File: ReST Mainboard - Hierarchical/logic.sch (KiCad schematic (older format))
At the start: 19 parts, among them IC1 AT24C256, P15 USB_OTG, U10 USBLC6-2, U9 STM32F10x/STM32F4x, X1 Crystal_Small

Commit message: started routing
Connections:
- net USB_D+ renamed USBP_D+
- net USB_D- renamed USBP_D-
- net USB_DM_- renamed USB_MCU-
- net USB_DP_+ renamed USB_MCU+
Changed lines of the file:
@@
 USB INTERFACE
 Text Label 9150 450  0    39   ~ 0
-USB_D+
+USBP_D+
 Text Label 9100 550  0    39   ~ 0
-USB_D-
+USBP_D-
 Text Label 10500 450  1    39   ~ 0
 USBR+
@@
 SPI_CS0
 Text GLabel 6700 1850 2    39   Input ~ 0
-USB_DP_+
+USB_MCU+
 Text GLabel 6700 1750 2    39   Input ~ 0
-USB_DM_-
+USB_MCU-
 $Comp
 L AT24C256 IC1
@@
 RESET
 Text GLabel 10900 450  2    39   Input ~ 0
-USB_DP_+
+USB_MCU+
 Text GLabel 10900 550  2    39   Input ~ 0
-USB_DM_-
+USB_MCU-
 Text GLabel 3700 1550 0    39   Input ~ 0
 P_VCAP_2

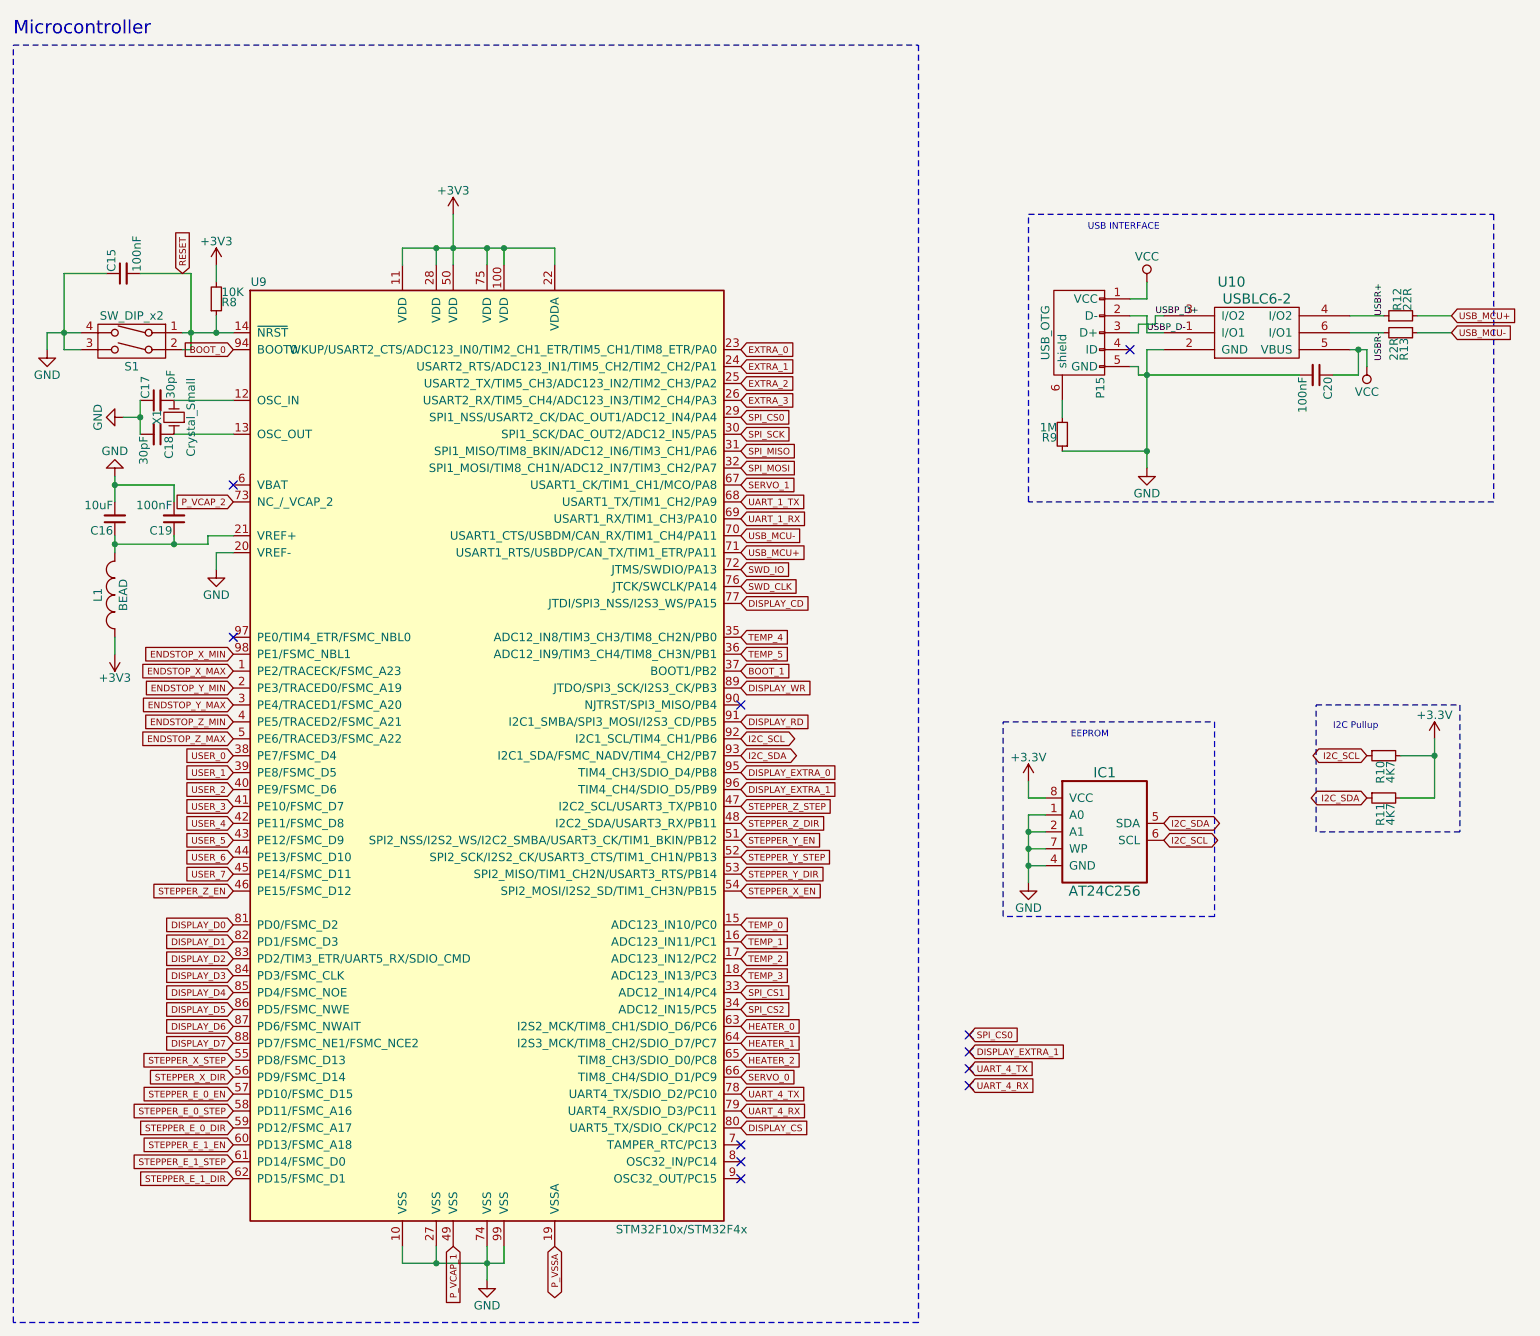
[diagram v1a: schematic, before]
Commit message: Mostly finished with main PCB. Only need to work the High Current Stuff out. On Vacation for now
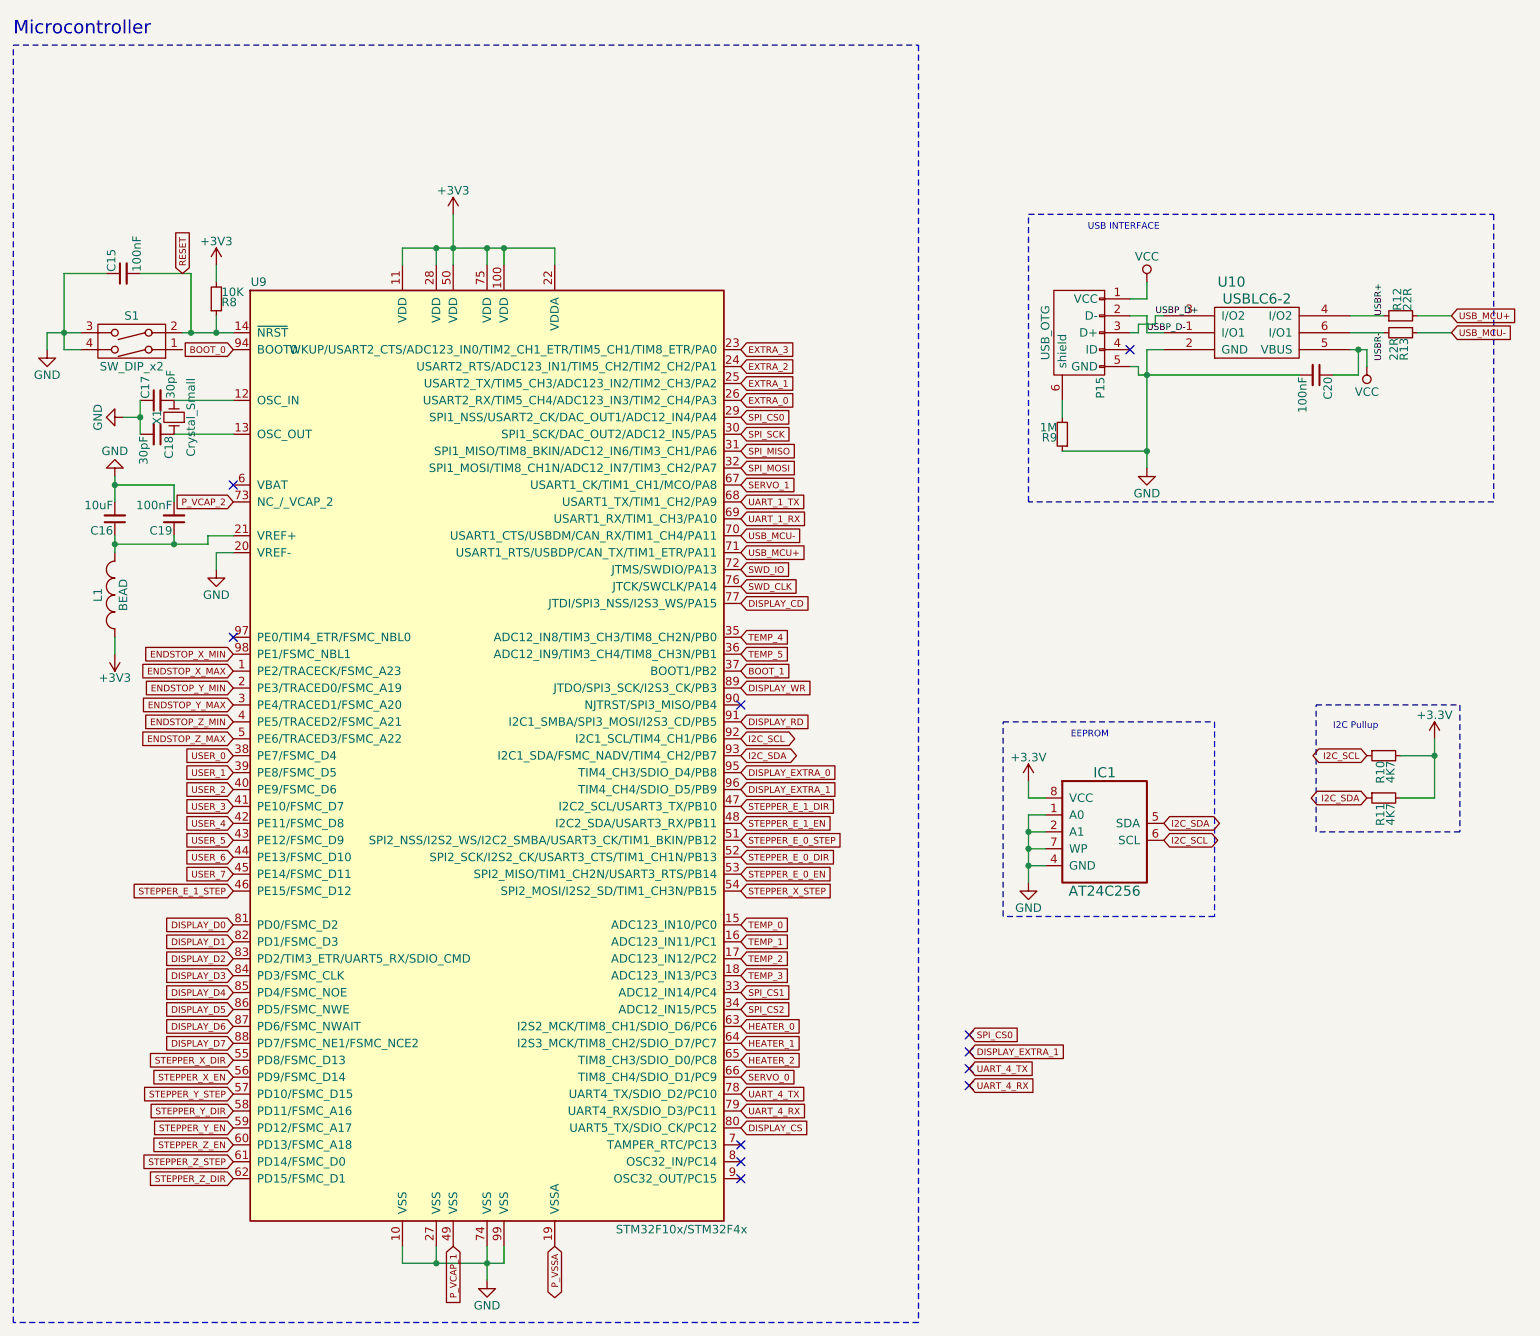
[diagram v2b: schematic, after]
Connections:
- net EXTRA_0: now also U9.26 (USART2_RX/TIM5_CH4/ADC123_IN3/TIM2_CH4/PA3); no longer U9.23 (WKUP/USART2_CTS/ADC123_IN0/TIM2_CH1_ETR/TIM5_CH1/TIM8_ETR/PA0)
- net EXTRA_1: now also U9.25 (USART2_TX/TIM5_CH3/ADC123_IN2/TIM2_CH3/PA2); no longer U9.24 (USART2_RTS/ADC123_IN1/TIM5_CH2/TIM2_CH2/PA1)
- net EXTRA_2: now also U9.24 (USART2_RTS/ADC123_IN1/TIM5_CH2/TIM2_CH2/PA1); no longer U9.25 (USART2_TX/TIM5_CH3/ADC123_IN2/TIM2_CH3/PA2)
- net EXTRA_3: now also U9.23 (WKUP/USART2_CTS/ADC123_IN0/TIM2_CH1_ETR/TIM5_CH1/TIM8_ETR/PA0); no longer U9.26 (USART2_RX/TIM5_CH4/ADC123_IN3/TIM2_CH4/PA3)
- net RESET: no longer S1.1
- net STEPPER_E_0_DIR: now also U9.52 (SPI2_SCK/I2S2_CK/USART3_CTS/TIM1_CH1N/PB13); no longer U9.59 (PD12/FSMC_A17)
- net STEPPER_E_0_EN: now also U9.53 (SPI2_MISO/TIM1_CH2N/USART3_RTS/PB14); no longer U9.57 (PD10/FSMC_D15)
- net STEPPER_E_0_STEP: now also U9.51 (SPI2_NSS/I2S2_WS/I2C2_SMBA/USART3_CK/TIM1_BKIN/PB12); no longer U9.58 (PD11/FSMC_A16)
- net STEPPER_E_1_DIR: now also U9.47 (I2C2_SCL/USART3_TX/PB10); no longer U9.62 (PD15/FSMC_D1)
- net STEPPER_E_1_EN: now also U9.48 (I2C2_SDA/USART3_RX/PB11); no longer U9.60 (PD13/FSMC_A18)
- net STEPPER_E_1_STEP: now also U9.46 (PE15/FSMC_D12); no longer U9.61 (PD14/FSMC_D0)
- net STEPPER_X_DIR: now also U9.55 (PD8/FSMC_D13); no longer U9.56 (PD9/FSMC_D14)
- net STEPPER_X_EN: now also U9.56 (PD9/FSMC_D14); no longer U9.54 (SPI2_MOSI/I2S2_SD/TIM1_CH3N/PB15)
- net STEPPER_X_STEP: now also U9.54 (SPI2_MOSI/I2S2_SD/TIM1_CH3N/PB15); no longer U9.55 (PD8/FSMC_D13)
- net STEPPER_Y_DIR: now also U9.58 (PD11/FSMC_A16); no longer U9.53 (SPI2_MISO/TIM1_CH2N/USART3_RTS/PB14)
- net STEPPER_Y_EN: now also U9.59 (PD12/FSMC_A17); no longer U9.51 (SPI2_NSS/I2S2_WS/I2C2_SMBA/USART3_CK/TIM1_BKIN/PB12)
- net STEPPER_Y_STEP: now also U9.57 (PD10/FSMC_D15); no longer U9.52 (SPI2_SCK/I2S2_CK/USART3_CTS/TIM1_CH1N/PB13)
- net STEPPER_Z_DIR: now also U9.62 (PD15/FSMC_D1); no longer U9.48 (I2C2_SDA/USART3_RX/PB11)
- net STEPPER_Z_EN: now also U9.60 (PD13/FSMC_A18); no longer U9.46 (PE15/FSMC_D12)
- net STEPPER_Z_STEP: now also U9.61 (PD14/FSMC_D0); no longer U9.47 (I2C2_SCL/USART3_TX/PB10)

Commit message: electrically finished. in the works of the silkscreening.
Schematic for SD Card Adapter and a RepRapDiscount-Adapter in the works. but not in this commit
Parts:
- P15: footprint Connect:USB_Mini-B -> ReST-Library:USB_Mini-B
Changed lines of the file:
@@
 F 0 "P15" H 9025 425 50  0000 C CNN
 F 1 "USB_OTG" H 8700 750 50  0000 C CNN
-F 2 "Connect:USB_Mini-B" V 8650 450 50  0001 C CNN
+F 2 "ReST-Library:USB_Mini-B" V 8650 450 50  0001 C CNN
 F 3 "" V 8650 450 50  0000 C CNN
 	1    8700 550

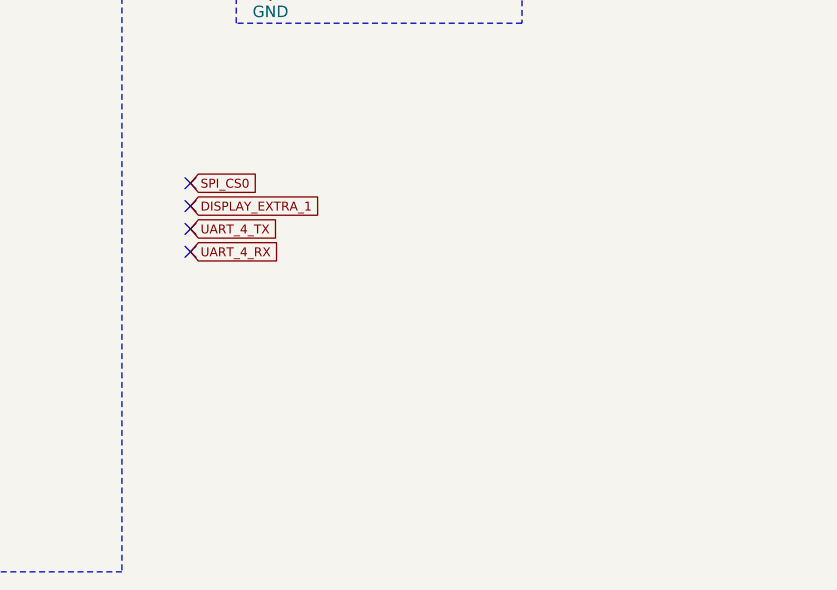
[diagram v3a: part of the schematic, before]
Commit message: added ESP-01 Support
Afterthought, completely forgot about it
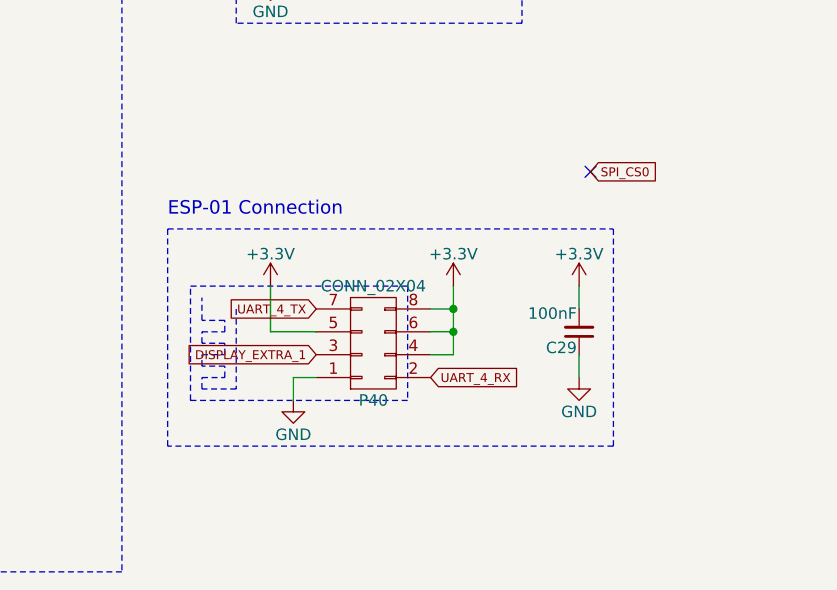
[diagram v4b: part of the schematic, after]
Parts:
- added C29: 100nF, Capacitors_SMD:C_0805_HandSoldering, symbol C_Small
- added P40: CONN_02X04, Pin_Headers:Pin_Header_Straight_2x04, symbol CONN_02X04
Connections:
- net +3V3: now also C29.2, P40.4 (P4), P40.5 (P5), P40.6 (P6), P40.8 (P8)
- net DISPLAY_EXTRA_1: now also P40.3 (P3)
- net GND: now also C29.1, P40.1 (P1)
- net UART_4_RX: now also P40.2 (P2)
- net UART_4_TX: now also P40.7 (P7)
- no-connect marks 11 -> 8
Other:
- note added: "ESP-01 Connection"
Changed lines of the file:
@@
 $EndDescr
 $Comp
-L +3.3V #PWR0120
+L +3.3V #PWR121
 U 1 1 5778C1BC
 P 8400 3200
-F 0 "#PWR0120" H 8400 3050 50  0001 C CNN
+F 0 "#PWR121" H 8400 3050 50  0001 C CNN
 F 1 "+3.3V" H 8400 3340 50  0000 C CNN
 F 2 "" H 8400 3200 50  0000 C CNN
@@
 $EndComp
 $Comp
-L GND #PWR0121
+L GND #PWR122
 U 1 1 5778C1C2
 P 8400 3800
-F 0 "#PWR0121" H 8400 3550 50  0001 C CNN
+F 0 "#PWR122" H 8400 3550 50  0001 C CNN
 F 1 "GND" H 8400 3650 50  0000 C CNN
 F 2 "" H 8400 3800 50  0000 C CNN
@@
 I2C_SDA
 $Comp
-L +3.3V #PWR0122
+L +3.3V #PWR131
 U 1 1 5778E907
 P 10800 2950
-F 0 "#PWR0122" H 10800 2800 50  0001 C CNN
+F 0 "#PWR131" H 10800 2800 50  0001 C CNN
 F 1 "+3.3V" H 10800 3090 50  0000 C CNN
 F 2 "" H 10800 2950 50  0000 C CNN
@@
 I2C_SDA
 $Comp
-L +3V3 #PWR0123
+L +3V3 #PWR119
 U 1 1 57791FB8
 P 5000 -150
-F 0 "#PWR0123" H 5000 -300 50  0001 C CNN
+F 0 "#PWR119" H 5000 -300 50  0001 C CNN
 F 1 "+3V3" H 5000 -10 50  0000 C CNN
 F 2 "" H 5000 -150 50  0000 C CNN
@@
 $EndComp
 $Comp
-L GND #PWR0124
+L GND #PWR116
 U 1 1 57791FBE
 P 3050 1050
-F 0 "#PWR0124" H 3050 800 50  0001 C CNN
+F 0 "#PWR116" H 3050 800 50  0001 C CNN
 F 1 "GND" H 3050 900 50  0000 C CNN
 F 2 "" H 3050 1050 50  0000 C CNN
@@
 $EndComp
 $Comp
-L GND #PWR0125
+L GND #PWR120
 U 1 1 57791FC4
 P 5200 6150
-F 0 "#PWR0125" H 5200 5900 50  0001 C CNN
+F 0 "#PWR120" H 5200 5900 50  0001 C CNN
 F 1 "GND" H 5200 6000 50  0000 C CNN
 F 2 "" H 5200 6150 50  0000 C CNN
@@
 $EndComp
 $Comp
-L GND #PWR0126
+L GND #PWR118
 U 1 1 57791FDF
 P 3600 1950
-F 0 "#PWR0126" H 3600 1700 50  0001 C CNN
+F 0 "#PWR118" H 3600 1700 50  0001 C CNN
 F 1 "GND" H 3600 1800 50  0000 C CNN
 F 2 "" H 3600 1950 50  0000 C CNN
@@
 $EndComp
 $Comp
-L +3V3 #PWR0127
+L +3V3 #PWR117
 U 1 1 57791FED
 P 3600 150
-F 0 "#PWR0127" H 3600 0   50  0001 C CNN
+F 0 "#PWR117" H 3600 0   50  0001 C CNN
 F 1 "+3V3" H 3600 290 50  0000 C CNN
 F 2 "" H 3600 150 50  0000 C CNN
@@
 $EndComp
 $Comp
-L GND #PWR0128
+L GND #PWR113
 U 1 1 57791FF3
 P 2600 650
-F 0 "#PWR0128" H 2600 400 50  0001 C CNN
+F 0 "#PWR113" H 2600 400 50  0001 C CNN
 F 1 "GND" H 2600 500 50  0000 C CNN
 F 2 "" H 2600 650 50  0000 C CNN
@@
 $EndComp
 $Comp
-L +3V3 #PWR0129
+L +3V3 #PWR115
 U 1 1 57792016
 P 3000 2450
-F 0 "#PWR0129" H 3000 2300 50  0001 C CNN
+F 0 "#PWR115" H 3000 2300 50  0001 C CNN
 F 1 "+3V3" H 3000 2590 50  0000 C CNN
 F 2 "" H 3000 2450 50  0000 C CNN
@@
 $EndComp
 $Comp
-L GND #PWR0130
+L GND #PWR114
 U 1 1 5779201C
 P 3000 1400
-F 0 "#PWR0130" H 3000 1150 50  0001 C CNN
+F 0 "#PWR114" H 3000 1150 50  0001 C CNN
 F 1 "GND" H 3000 1250 50  0000 C CNN
 F 2 "" H 3000 1400 50  0000 C CNN
@@
 $EndComp
 $Comp
-L GND #PWR0131
+L GND #PWR126
 U 1 1 577937EA
 P 9100 1350
-F 0 "#PWR0131" H 9100 1100 50  0001 C CNN
+F 0 "#PWR126" H 9100 1100 50  0001 C CNN
 F 1 "GND" H 9100 1200 50  0000 C CNN
 F 2 "" H 9100 1350 50  0000 C CNN
@@
 $EndComp
 $Comp
-L VCC #PWR0132
+L VCC #PWR125
 U 1 1 57793807
 P 9100 250
-F 0 "#PWR0132" H 9100 100 50  0001 C CNN
+F 0 "#PWR125" H 9100 100 50  0001 C CNN
 F 1 "VCC" H 9100 400 50  0000 C CNN
 F 2 "" H 9100 250 50  0000 C CNN
@@
 $EndComp
 $Comp
-L VCC #PWR0133
+L VCC #PWR130
 U 1 1 5779380D
 P 10400 750
-F 0 "#PWR0133" H 10400 600 50  0001 C CNN
+F 0 "#PWR130" H 10400 600 50  0001 C CNN
 F 1 "VCC" H 10400 900 50  0000 C CNN
 F 2 "" H 10400 750 50  0000 C CNN
@@
 Text GLabel 5600 5950 3    39   BiDi ~ 0
 P_VSSA
-Text GLabel 8050 5000 2    39   Input ~ 0
+Text GLabel 9100 5550 2    39   Input ~ 0
 UART_4_RX
-Text GLabel 8050 4900 2    39   Input ~ 0
+Text GLabel 8600 5250 0    39   Input ~ 0
 UART_4_TX
-NoConn ~ 8050 4900
-NoConn ~ 8050 5000
-Text GLabel 8050 4800 2    39   Input ~ 0
+Text GLabel 8600 5450 0    39   Input ~ 0
 DISPLAY_EXTRA_1
-NoConn ~ 8050 4800
-Text GLabel 8050 4700 2    39   Input ~ 0
+Text GLabel 9800 4650 2    39   Input ~ 0
 SPI_CS0
-NoConn ~ 8050 4700
+$Comp
+L CONN_02X04 P40
+U 1 1 5797F867
+P 8850 5400
+F 0 "P40" H 8850 5650 50  0000 C CNN
+F 1 "CONN_02X04" H 8850 5150 50  0000 C CNN
+F 2 "Pin_Headers:Pin_Header_Straight_2x04" H 8850 4200 50  0001 C CNN
+F 3 "" H 8850 4200 50  0000 C CNN
+	1    8850 5400
+	1    0    0    1
+$EndComp
+$Comp
+L +3.3V #PWR127
+U 1 1 5797FE7C
+P 9200 5150
+F 0 "#PWR127" H 9200 5000 50  0001 C CNN
+F 1 "+3.3V" H 9200 5290 50  0000 C CNN
+F 2 "" H 9200 5150 50  0000 C CNN
+F 3 "" H 9200 5150 50  0000 C CNN
+	1    9200 5150
+	1    0    0    -1
+$EndComp
+$Comp
+L GND #PWR124
+U 1 1 5797FEC3
+P 8500 5650
+F 0 "#PWR124" H 8500 5400 50  0001 C CNN
+F 1 "GND" H 8500 5500 50  0000 C CNN
+F 2 "" H 8500 5650 50  0000 C CNN
+F 3 "" H 8500 5650 50  0000 C CNN
+	1    8500 5650
+	1    0    0    -1
+$EndComp
+$Comp
+L C_Small C29
+U 1 1 5798094C
+P 9750 5350
+F 0 "C29" H 9760 5420 50  0000 L CNN
+F 1 "100nF" H 9760 5270 50  0000 L CNN
+F 2 "Capacitors_SMD:C_0805_HandSoldering" H 9750 5350 50  0001 C CNN
+F 3 "" H 9750 5350 50  0000 C CNN
+	1    9750 5350
+	-1   0    0    1
+$EndComp
+NoConn ~ 9800 4650
+$Comp
+L +3.3V #PWR128
+U 1 1 57980B54
+P 9750 5150
+F 0 "#PWR128" H 9750 5000 50  0001 C CNN
+F 1 "+3.3V" H 9750 5290 50  0000 C CNN
+F 2 "" H 9750 5150 50  0000 C CNN
+F 3 "" H 9750 5150 50  0000 C CNN
+	1    9750 5150
+	1    0    0    -1
+$EndComp
+$Comp
+L GND #PWR129
+U 1 1 57980B9E
+P 9750 5550
+F 0 "#PWR129" H 9750 5300 50  0001 C CNN
+F 1 "GND" H 9750 5400 50  0000 C CNN
+F 2 "" H 9750 5550 50  0000 C CNN
+F 3 "" H 9750 5550 50  0000 C CNN
+	1    9750 5550
+	1    0    0    -1
+$EndComp
 Wire Notes Line
 	8250 4000 8250 2850
@@
 	3450 550  3450 200
 Connection ~ 3450 550
+Wire Wire Line
+	8500 5650 8500 5550
+Wire Wire Line
+	8500 5550 8600 5550
+Wire Wire Line
+	9200 5150 9200 5450
+Wire Wire Line
+	9200 5250 9100 5250
+Wire Wire Line
+	9750 5550 9750 5450
+Wire Wire Line
+	9750 5250 9750 5150
+Wire Notes Line
+	9000 5650 8050 5650
+Wire Notes Line
+	8050 5650 8050 5150
+Wire Notes Line
+	8050 5150 9000 5150
+Wire Notes Line
+	9000 5150 9000 5650
+Wire Notes Line
+	8250 5250 8250 5600
+Wire Notes Line
+	8250 5600 8100 5600
+Wire Notes Line
+	8100 5600 8100 5550
+Wire Notes Line
+	8100 5550 8200 5550
+Wire Notes Line
+	8200 5550 8200 5500
+Wire Notes Line
+	8200 5500 8100 5500
+Wire Notes Line
+	8100 5500 8100 5450
+Wire Notes Line
+	8100 5450 8200 5450
+Wire Notes Line
+	8200 5450 8200 5400
+Wire Notes Line
+	8200 5400 8100 5400
+Wire Notes Line
+	8100 5400 8100 5350
+Wire Notes Line
+	8100 5350 8200 5350
+Wire Notes Line
+	8200 5350 8200 5300
+Wire Notes Line
+	8200 5300 8100 5300
+Wire Notes Line
+	8100 5300 8100 5200
+Wire Wire Line
+	9200 5450 9100 5450
+Connection ~ 9200 5250
+Wire Wire Line
+	8400 5350 8600 5350
+$Comp
+L +3.3V #PWR123
+U 1 1 57983B6D
+P 8400 5150
+F 0 "#PWR123" H 8400 5000 50  0001 C CNN
+F 1 "+3.3V" H 8400 5290 50  0000 C CNN
+F 2 "" H 8400 5150 50  0000 C CNN
+F 3 "" H 8400 5150 50  0000 C CNN
+	1    8400 5150
+	1    0    0    -1
+$EndComp
+Wire Wire Line
+	8400 5150 8400 5350
+Wire Wire Line
+	9100 5350 9200 5350
+Connection ~ 9200 5350
+Wire Notes Line
+	7950 4900 9900 4900
+Wire Notes Line
+	9900 4900 9900 5850
+Wire Notes Line
+	9900 5850 7950 5850
+Wire Notes Line
+	7950 5850 7950 4900
+Text Notes 7950 4850 0    59   ~ 0
+ESP-01 Connection
 $EndSCHEMATC
